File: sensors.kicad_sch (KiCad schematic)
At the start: 6 parts, among them U3 BMP390, U4 LSM6DSO32TR

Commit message: bozza layout pcb
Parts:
- added C29, C30: 100nF, Capacitor_SMD:C_0603_1608Metric_Pad1.08x0.95mm_HandSolder, symbol Device:C
- added C33: 220n, Capacitor_SMD:C_0603_1608Metric_Pad1.08x0.95mm_HandSolder, symbol Device:C
- added C34, C36: 100n, Capacitor_SMD:C_0603_1608Metric_Pad1.08x0.95mm_HandSolder, symbol Device:C
- added C35: 10u, Capacitor_SMD:C_0603_1608Metric_Pad1.08x0.95mm_HandSolder, symbol Device:C
- added U7: LSM6DSO32TR, LSM6DSO32TR:LGA-14L_2P5X3X0P83_STM-M, symbol 2024-10-18_09-38-35:LSM6DSO32TR
- added U8: LIS2MDL, Package_LGA:LGA-12_2x2mm_P0.5mm, symbol Sensor_Magnetic:LIS2MDL
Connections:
- net +3.3V: now also C29.2, C30.2, U7.5 (VDDIO), U7.8 (VDD)
- net CK: now also U7.13 (SCL), U8.1 (SCL/SPC)
- net GND: now also C29.1, C30.1, C33.2, C34.2, C35.2, C36.1, U7.6 (GND), U7.7 (GND), U8.6 (GND), U8.8 (GND)
- net RX: now also U7.1 (SDO/SA0), U8.7 (DRDY)
- net SPI1.TX: now also U7.14 (SDA), U8.4 (SDA/SDI/SDO)
- new net: C33.1, U8.5 (C1)
- new net +3V3: C34.1, C35.1, C36.2, U8.10 (Vdd_IO), U8.9 (Vdd)
- new net IMU45_CS: U7.12 (CS)
- new net IMU45_INT1: U7.4 (INT1)
- new net IMU45_INT2: U7.9 (INT2)
- new net MAG_CS: U8.3 (~{CS})
- no-connect marks 2 -> 4
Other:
- note added: "LIS2MDL eCompass"
- note added: "LSM6DSO32 IMU 45 module"
- moved on the sheet: C25, C26, C27, C28, U3, U4

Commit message: Corrections
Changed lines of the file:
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@@
 		(on_board yes)
 		(dnp no)
-		(fields_autoplaced yes)
 		(property "Reference" "U8"
-			(at 211.6933 144.78 0)
+			(at 194.31 142.24 0)
 			(effects
 				(font
@@
 		)
 		(property "Value" "LIS2MDL"
-			(at 211.6933 147.32 0)
+			(at 194.31 144.78 0)
 			(effects
 				(font

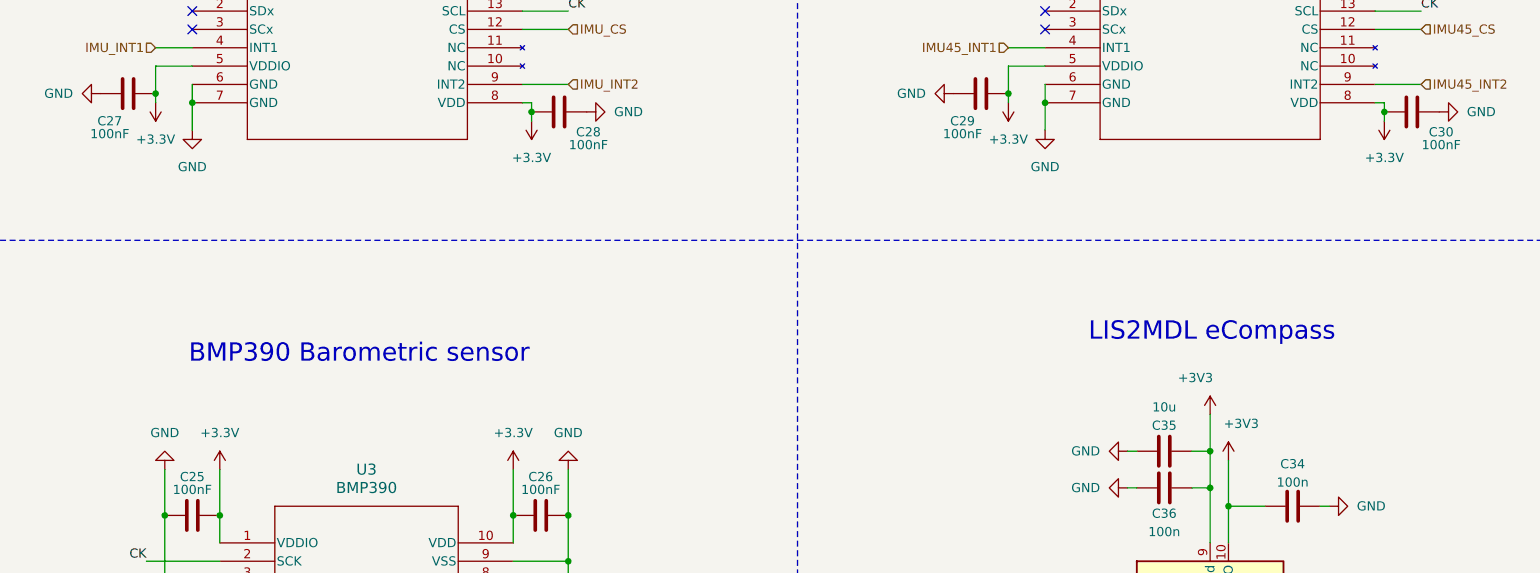
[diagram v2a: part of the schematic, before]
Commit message: NET allignment (all on +3V3)
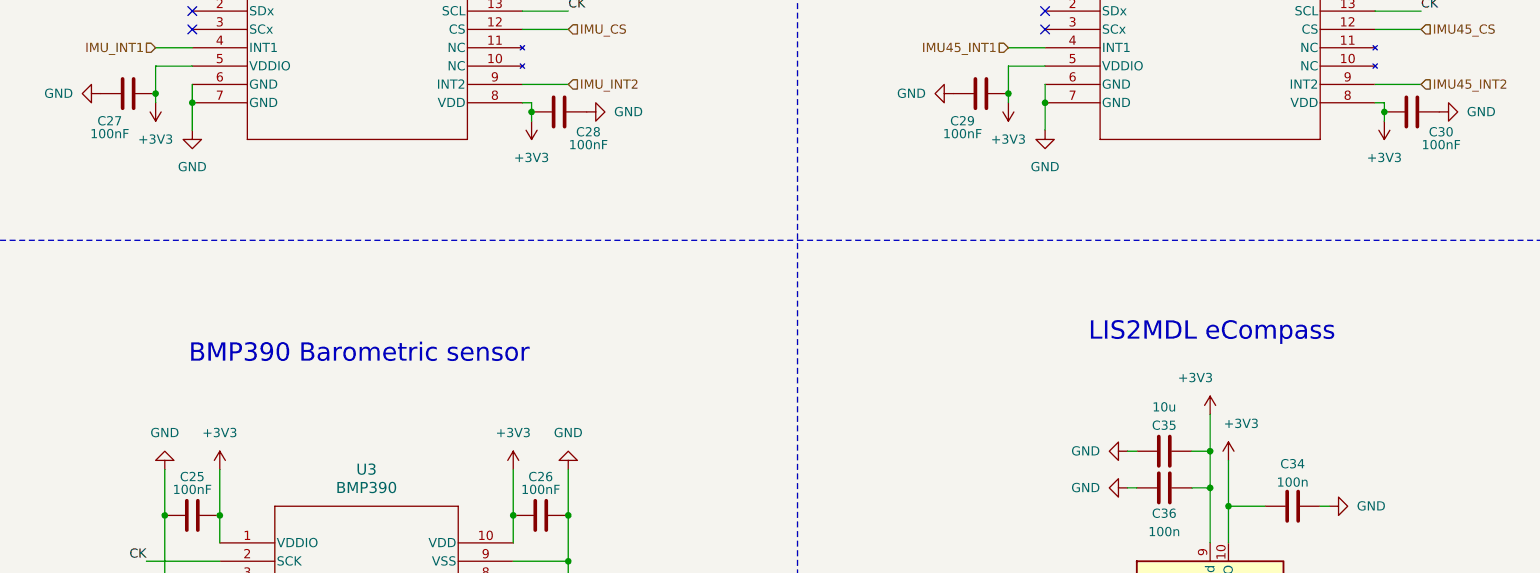
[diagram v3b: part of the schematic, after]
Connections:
- net +3.3V is gone; now on net +3V3: C25.2, C26.1, C27.2, C28.2, C29.2, C30.2, U3.1 (VDDIO), U3.10 (VDD), U4.5 (VDDIO), U4.8 (VDD), U7.5 (VDDIO), U7.8 (VDD)
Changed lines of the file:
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@@
 			)
 		)
-		(property "Value" "+3.3V"
+		(property "Value" "+3V3"
 			(at 63.5 63.5 0)
 			(effects
@@
 			)
 		)
-		(property "Description" "Power symbol creates a global label with name \"+3.3V\""
+		(property "Description" "Power symbol creates a global label with name \"+3V3\""
 			(at 63.5 58.42 0)
 			(effects
@@
 			)
 		)
-		(property "Value" "+3.3V"
+		(property "Value" "+3V3"
 			(at 181.61 63.5 0)
 			(effects
@@
 			)
 		)
-		(property "Description" "Power symbol creates a global label with name \"+3.3V\""
+		(property "Description" "Power symbol creates a global label with name \"+3V3\""
 			(at 181.61 58.42 0)
 			(effects
@@
 			)
 		)
-		(property "Value" "+3.3V"
+		(property "Value" "+3V3"
 			(at 113.03 104.14 0)
 			(effects
@@
 			)
 		)
-		(property "Description" "Power symbol creates a global label with name \"+3.3V\""
+		(property "Description" "Power symbol creates a global label with name \"+3V3\""
 			(at 113.03 109.22 0)
 			(effects
@@
 			)
 		)
-		(property "Value" "+3.3V"
+		(property "Value" "+3V3"
 			(at 115.57 66.04 0)
 			(effects
@@
 			)
 		)
-		(property "Description" "Power symbol creates a global label with name \"+3.3V\""
+		(property "Description" "Power symbol creates a global label with name \"+3V3\""
 			(at 115.57 60.96 0)
 			(effects
@@
 			)
 		)
-		(property "Value" "+3.3V"
+		(property "Value" "+3V3"
 			(at 233.68 66.04 0)
 			(effects
@@
 			)
 		)
-		(property "Description" "Power symbol creates a global label with name \"+3.3V\""
+		(property "Description" "Power symbol creates a global label with name \"+3V3\""
 			(at 233.68 60.96 0)
 			(effects
@@
 			)
 		)
-		(property "Value" "+3.3V"
+		(property "Value" "+3V3"
 			(at 72.39 104.14 0)
 			(effects
@@
 			)
 		)
-		(property "Description" "Power symbol creates a global label with name \"+3.3V\""
+		(property "Description" "Power symbol creates a global label with name \"+3V3\""
 			(at 72.39 109.22 0)
 			(effects

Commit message: New GPS and sensors
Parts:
- removed C25, C26: 100nF, Capacitor_SMD:C_0603_1608Metric_Pad1.08x0.95mm_HandSolder, symbol Device:C
- removed U3: BMP390, bmp390:10LGA_2X2X0p75_BOS-M, symbol bmp390:BMP390
- added C38: 100nF, symbol Device:C
- added U11: LPS22DF, Package_LGA:ST_HLGA-10_2x2mm_P0.5mm_LayoutBorder3x2y, symbol Sensor_Pressure:LPS22DF
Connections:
- net +3V3: now also C38.1, U11.1 (Vdd_IO), U11.10 (VDD)
- net BARO_CS: now also U11.6 (~{CS})
- net BARO_INT: now also U11.7 (INT_DRDY)
- net CK: now also U11.2 (SCL)
- net GND: now also C38.2, U11.3 (GND), U11.8 (GND_IO), U11.9 (GND)
- net RX: now also U11.5 (SA0)
- net SPI1.TX renamed TX
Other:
- note added: "LPS22DS Barometer"
- note removed: "BMP390 Barometric sensor"

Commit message: LIV5
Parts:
- C38: footprint (none) -> Capacitor_SMD:C_0603_1608Metric_Pad1.08x0.95mm_HandSolder
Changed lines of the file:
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@@
 			)
 		)
-		(property "Footprint" ""
+		(property "Footprint" "Capacitor_SMD:C_0603_1608Metric_Pad1.08x0.95mm_HandSolder"
 			(at 70.0532 123.444 0)
 			(effects

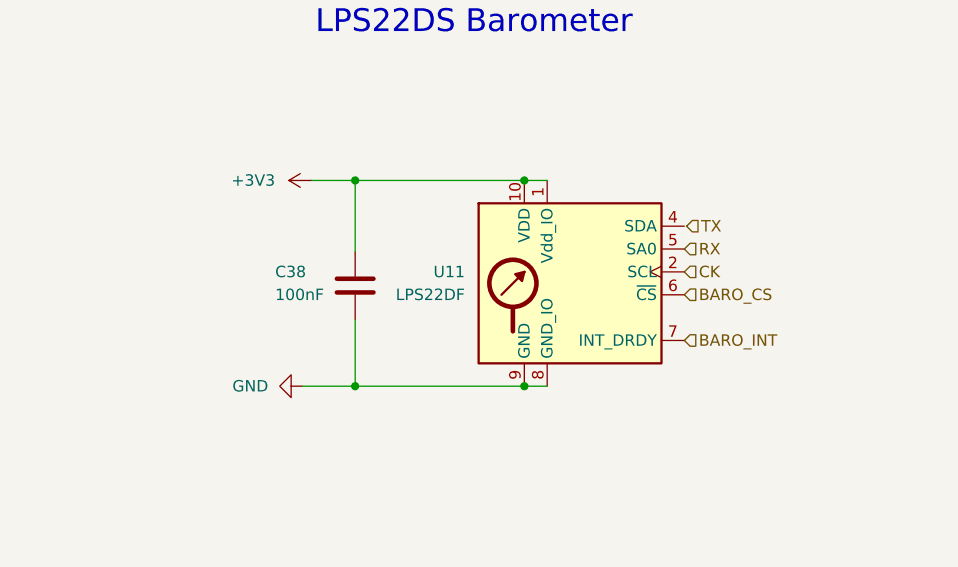
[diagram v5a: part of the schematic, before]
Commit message: mega routing sensori led e 5v usb
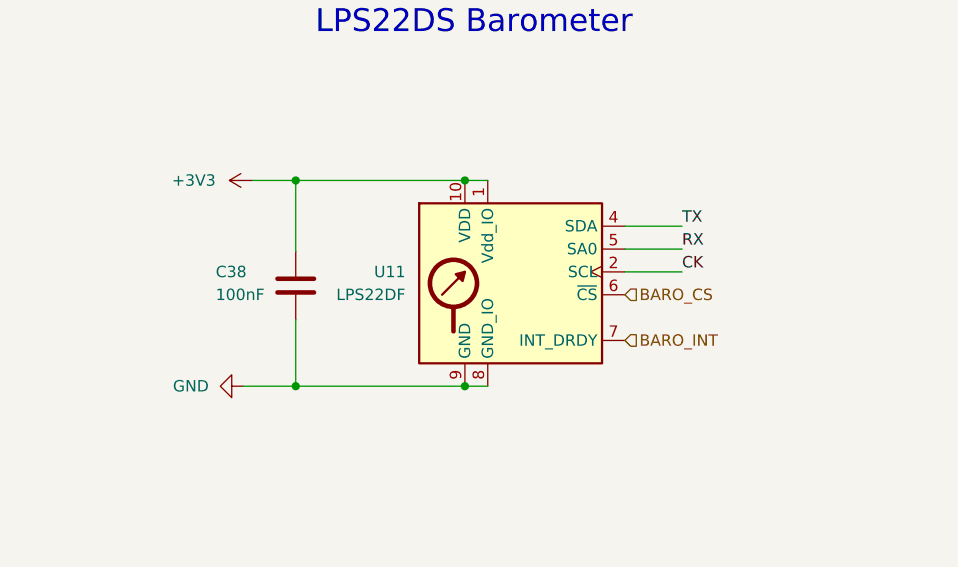
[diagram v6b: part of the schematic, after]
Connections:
- net TX is gone; now on net SPI1.TX: U4.14 (SDA), U7.14 (SDA), U8.4 (SDA/SDI/SDO)
- net SPI1.TX: now reaches U11.4 (SDA)
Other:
- moved on the sheet: C38, U11
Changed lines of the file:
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@@
 	)
 	(junction
-		(at 87.884 107.95)
+		(at 81.28 107.95)
 		(diameter 0)
 		(color 0 0 0 0)
@@
 	)
 	(junction
-		(at 69.088 130.81)
+		(at 62.484 130.81)
 		(diameter 0)
 		(color 0 0 0 0)
 	)
 	(junction
-		(at 87.884 130.81)
+		(at 81.28 130.81)
 		(diameter 0)
 		(color 0 0 0 0)
@@
 	)
 	(junction
-		(at 69.088 107.95)
+		(at 62.484 107.95)
 		(diameter 0)
 		(color 0 0 0 0)
@@
 	(wire
 		(pts
-			(xy 69.088 107.95) (xy 69.088 115.824)
+			(xy 62.484 107.95) (xy 62.484 115.824)
 		)
 		(stroke
@@
 	(wire
 		(pts
-			(xy 69.088 130.81) (xy 87.884 130.81)
+			(xy 105.41 115.57) (xy 99.06 115.57)
 		)
 		(stroke
@@
 	(wire
 		(pts
-			(xy 63.246 130.81) (xy 69.088 130.81)
+			(xy 62.484 130.81) (xy 81.28 130.81)
+		)
+		(stroke
+			(width 0)
+			(type default)
+		)
+	)
+	(wire
+		(pts
+			(xy 56.642 130.81) (xy 62.484 130.81)
 		)
 		(stroke
@@
 	(wire
 		(pts
-			(xy 90.424 107.95) (xy 87.884 107.95)
+			(xy 105.41 118.11) (xy 99.06 118.11)
+		)
+		(stroke
+			(width 0)
+			(type default)
+		)
+	)
+	(wire
+		(pts
+			(xy 83.82 107.95) (xy 81.28 107.95)
 		)
 		(stroke
@@
 	(wire
 		(pts
-			(xy 64.262 107.95) (xy 69.088 107.95)
+			(xy 105.41 113.03) (xy 99.06 113.03)
+		)
+		(stroke
+			(width 0)
+			(type default)
+		)
+	)
+	(wire
+		(pts
+			(xy 57.658 107.95) (xy 62.484 107.95)
 		)
 		(stroke
@@
 	(wire
 		(pts
-			(xy 87.884 130.81) (xy 90.424 130.81)
+			(xy 81.28 130.81) (xy 83.82 130.81)
 		)
 		(stroke
@@
 	(wire
 		(pts
-			(xy 69.088 107.95) (xy 87.884 107.95)
+			(xy 62.484 107.95) (xy 81.28 107.95)
 		)
 		(stroke
@@
 	(wire
 		(pts
-			(xy 69.088 123.444) (xy 69.088 130.81)
+			(xy 62.484 123.444) (xy 62.484 130.81)
 		)
 		(stroke
@@
 		)
 	)
+	(label "RX"
+		(at 105.41 115.57 0)
+		(effects
+			(font
+				(size 1.27 1.27)
+			)
+			(justify left bottom)
+		)
+	)
 	(label "CK"
 		(at 238.76 45.72 0)
@@
 		)
 	)
+	(label "CK"
+		(at 105.41 118.11 0)
+		(effects
+			(font
+				(size 1.27 1.27)
+			)
+			(justify left bottom)
+		)
+	)
 	(label "RX"
 		(at 115.57 173.99 0)
@@
 		)
 	)
+	(label "TX"
+		(at 105.41 113.03 0)
+		(effects
+			(font
+				(size 1.27 1.27)
+			)
+			(justify left bottom)
+		)
+	)
 	(label "SPI1.CK"
 		(at 102.87 176.53 0)
@@
 		)
 	)
-	(hierarchical_label "CK"
-		(shape input)
-		(at 105.664 118.11 0)
-		(effects
-			(font
-				(size 1.27 1.27)
-			)
-			(justify left)
-		)
-	)
 	(hierarchical_label "IMU45_CS"
 		(shape input)
@@
 	(hierarchical_label "BARO_INT"
 		(shape input)
-		(at 105.664 125.73 0)
+		(at 99.06 125.73 0)
 		(effects
 			(font
@@
 	(hierarchical_label "BARO_CS"
 		(shape input)
-		(at 105.664 120.65 0)
-		(effects
-			(font
-				(size 1.27 1.27)
-			)
-			(justify left)
-		)
-	)
-	(hierarchical_label "RX"
-		(shape input)
-		(at 105.664 115.57 0)
+		(at 99.06 120.65 0)
 		(effects
 			(font
@@
 		)
 	)
-	(hierarchical_label "TX"
-		(shape input)
-		(at 105.918 113.03 0)
-		(effects
-			(font
-				(size 1.27 1.27)
-			)
-			(justify left)
-		)
-	)
 	(symbol
 		(lib_id "Device:C")
@@
 	(symbol
 		(lib_id "Sensor_Pressure:LPS22DF")
-		(at 92.964 120.65 0)
+		(at 86.36 120.65 0)
 		(unit 1)
 		(exclude_from_sim no)
@@
 		(fields_autoplaced yes)
 		(property "Reference" "U11"
-			(at 81.28 118.1099 0)
+			(at 74.676 118.1099 0)
 			(effects
 				(font
@@
 		)
 		(property "Value" "LPS22DF"
-			(at 81.28 120.6499 0)
+			(at 74.676 120.6499 0)
 			(effects
 				(font
@@
 		)
 		(property "Footprint" "Package_LGA:ST_HLGA-10_2x2mm_P0.5mm_LayoutBorder3x2y"
-			(at 91.694 129.54 0)
+			(at 85.09 129.54 0)
 			(effects
 				(font
@@
 		)
 		(property "Datasheet" "https://www.st.com/resource/en/datasheet/lps22df.pdf"
-			(at 91.694 132.08 0)
+			(at 85.09 132.08 0)
 			(effects
 				(font
@@
 		)
 		(property "Description" "MEMS absolute pressure sensor, 260-1260 hPa, 1-200Hz ODR, 24bit, I2C/I3C/SPI interface, 2x2mm ST_HLGA-10L"
-			(at 92.964 120.65 0)
+			(at 86.36 120.65 0)
 			(effects
 				(font
@@
 	(symbol
 		(lib_id "power:GND")
-		(at 63.246 130.81 270)
+		(at 56.642 130.81 270)
 		(unit 1)
 		(exclude_from_sim no)
@@
 		(fields_autoplaced yes)
 		(property "Reference" "#PWR0117"
-			(at 56.896 130.81 0)
+			(at 50.292 130.81 0)
 			(effects
 				(font
@@
 		)
 		(property "Value" "GND"
-			(at 59.436 130.8099 90)
+			(at 52.832 130.8099 90)
 			(effects
 				(font
@@
 		)
 		(property "Footprint" ""
-			(at 63.246 130.81 0)
+			(at 56.642 130.81 0)
 			(effects
 				(font
@@
 		)
 		(property "Datasheet" ""
-			(at 63.246 130.81 0)
+			(at 56.642 130.81 0)
 			(effects
 				(font
@@
 		)
 		(property "Description" "Power symbol creates a global label with name \"GND\" , ground"
-			(at 63.246 130.81 0)
+			(at 56.642 130.81 0)
 			(effects
 				(font
@@
 	(symbol
 		(lib_id "power:+3V3")
-		(at 64.262 107.95 90)
+		(at 57.658 107.95 90)
 		(unit 1)
 		(exclude_from_sim no)
@@
 		(fields_autoplaced yes)
 		(property "Reference" "#PWR0103"
-			(at 68.072 107.95 0)
+			(at 61.468 107.95 0)
 			(effects
 				(font
@@
 		)
 		(property "Value" "+3V3"
-			(at 60.198 107.9499 90)
+			(at 53.594 107.9499 90)
 			(effects
 				(font
@@
 		)
 		(property "Footprint" ""
-			(at 64.262 107.95 0)
+			(at 57.658 107.95 0)
 			(effects
 				(font
@@
 		)
 		(property "Datasheet" ""
-			(at 64.262 107.95 0)
+			(at 57.658 107.95 0)
 			(effects
 				(font
@@
 		)
 		(property "Description" "Power symbol creates a global label with name \"+3V3\""
-			(at 64.262 107.95 0)
+			(at 57.658 107.95 0)
 			(effects
 				(font
@@
 	(symbol
 		(lib_id "Device:C")
-		(at 69.088 119.634 0)
+		(at 62.484 119.634 0)
 		(unit 1)
 		(exclude_from_sim no)
@@
 		(dnp no)
 		(property "Reference" "C38"
-			(at 60.198 118.11 0)
+			(at 53.594 118.11 0)
 			(effects
 				(font
@@
 		)
 		(property "Value" "100nF"
-			(at 60.198 120.65 0)
+			(at 53.594 120.65 0)
 			(effects
 				(font
@@
 		)
 		(property "Footprint" "Capacitor_SMD:C_0603_1608Metric_Pad1.08x0.95mm_HandSolder"
-			(at 70.0532 123.444 0)
+			(at 63.4492 123.444 0)
 			(effects
 				(font
@@
 		)
 		(property "Datasheet" "~"
-			(at 69.088 119.634 0)
+			(at 62.484 119.634 0)
 			(effects
 				(font
@@
 		)
 		(property "Description" "Unpolarized capacitor"
-			(at 69.088 119.634 0)
+			(at 62.484 119.634 0)
 			(effects
 				(font

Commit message: ROBE
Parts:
- removed U4, U7: LSM6DSO32TR, LSM6DSO32TR:LGA-14L_2P5X3X0P83_STM-M, symbol 2024-10-18_09-38-35:LSM6DSO32TR
- added U4, U5: LSM6DSV80XTR, lsm6dsv80x:QFN_LSM6DSV80XTR_STM, symbol lsm6dsv80x:LSM6DSV80XTR
- U11: footprint Package_LGA:ST_HLGA-10_2x2mm_P0.5mm_LayoutBorder3x2y -> LPS22DF:ST_HLGA-10_2x2mm_P0.5mm_LayoutBorder3x2y
- U8: footprint Package_LGA:LGA-12_2x2mm_P0.5mm -> LIS2MDL:LGA-12_2x2mm_P0.5mm
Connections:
- net +3V3: now also U4.5, U4.8, U5.5, U5.8
- net CK: now also U4.13, U5.13
- net GND: now also U4.6, U4.7, U5.6, U5.7
- net IMU45_CS: now also U4.12
- net IMU45_INT1: now also U4.4
- net IMU45_INT2: now also U4.9
- net IMU_CS: now also U5.12
- net IMU_INT1: now also U5.4
- net IMU_INT2: now also U5.9
- net RX: now also U4.1, U5.1; no longer U8.7 (DRDY)
- net SPI1.TX: now also U4.14, U5.14
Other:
- moved on the sheet: C27, C29

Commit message: Names fix
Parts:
- C33: value 220n -> 220nf
- C34, C36: value 100n -> 100nf
- C35: value 10u -> 10uf
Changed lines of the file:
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@@
 			)
 		)
-		(property "Value" "220n"
+		(property "Value" "220nf"
 			(at 228.6 139.6999 0)
 			(effects
@@
 			)
 		)
-		(property "Value" "100n"
+		(property "Value" "100nf"
 			(at 220.98 110.998 90)
 			(effects
@@
 			)
 		)
-		(property "Value" "10u"
+		(property "Value" "10uf"
 			(at 203.2 100.584 90)
 			(effects
@@
 			)
 		)
-		(property "Value" "100n"
+		(property "Value" "100nf"
 			(at 203.2 117.856 90)
 			(effects
